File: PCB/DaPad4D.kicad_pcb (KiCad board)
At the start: 2 copper layers, 100 x 19.1 mm, 14 parts, among them J1 Conn_01x12, SW1 SW_Push, SW2 SW_Push, SW3 SW_Push, SW4 SW_Push, SW5 Rotary_Encoder_Switch

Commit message: Moved files
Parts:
- added C3: C, Capacitor_SMD:C_0805_2012Metric_Pad1.15x1.40mm_HandSolder, F.Cu at (137.0, 65.0)
- added C4: C, Capacitor_SMD:C_0805_2012Metric_Pad1.15x1.40mm_HandSolder, F.Cu at (141.8, 65.0)
- added D7: 1N4148W, Diode_SMD:D_SOD-123, F.Cu at (136.5, 56.7)
- added H1: Hole, MountingHole:MountingHole_2.7mm_M2.5, B.Cu at (66.3, 64.0)
- added H2: Hole, MountingHole:MountingHole_2.7mm_M2.5, B.Cu at (123.8, 64.0)
- moved C2 11.5 mm to (141.8, 65.0), turned to 0 degrees
- moved C1 5.86 mm to (137.0, 65.0), turned to 0 degrees
- moved D2 5.38 mm to (136.5, 56.7), turned to 0 degrees
- moved J1 1.88 mm to (130.3, 67.3)
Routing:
- net Col5: track 3.32 -> 6.66 mm, vias 0 -> 1
- net VCC: track 87.4 -> 90.3 mm
- net Net-(D2-Pad2): track 12.0 -> 10.1 mm
- net Col2: track 61.4 -> 63.3 mm
- net Col1: track 79.8 -> 81.7 mm
- net RGB_IN: track 14.1 -> 16.0 mm
- net Row1: track 61.9 -> 60.3 mm
- net RGB_OUT: track 86.7 -> 88.3 mm
- net D1: track 18.6 -> 20.1 mm, vias 0 -> 1
- net Col3: track 42.8 -> 44.2 mm
- net D0: track 11.1 -> 11.8 mm, vias 0 -> 1
- net Col4: track 23.9 -> 24.6 mm
- net Net-(C1-Pad2): track 12.1 -> 11.4 mm

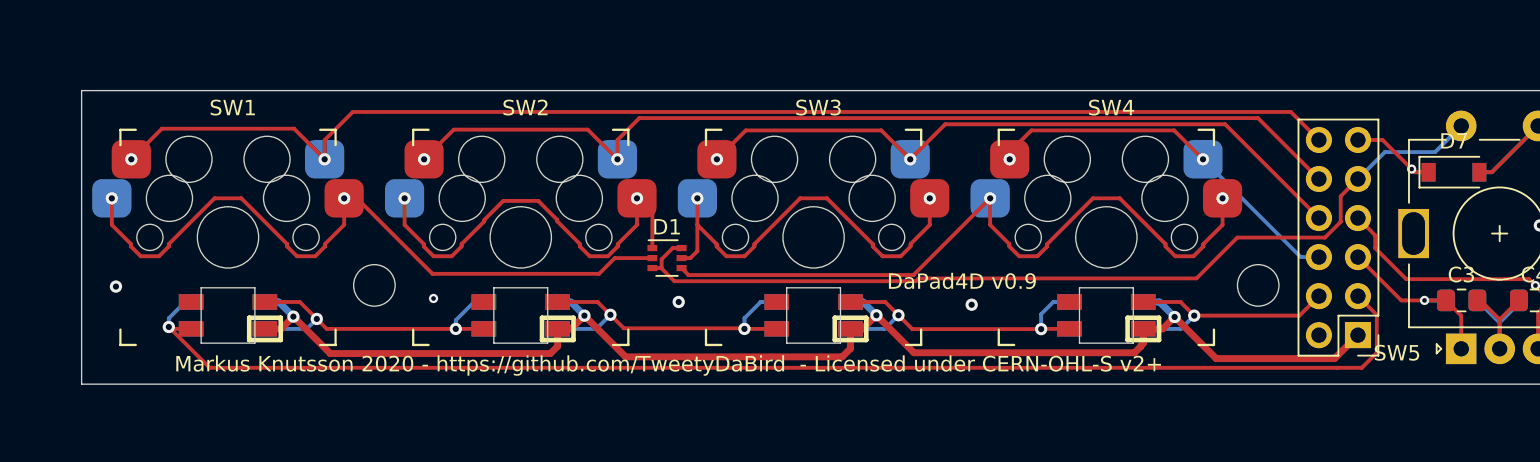
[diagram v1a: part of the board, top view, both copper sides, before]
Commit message: Cleaned up library dependencies
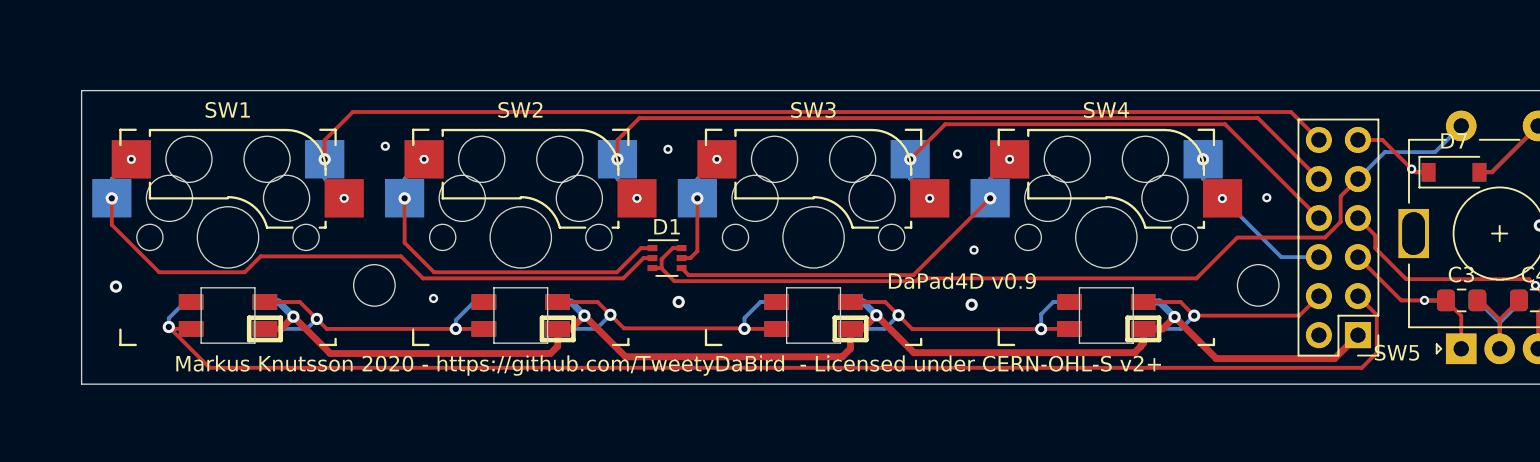
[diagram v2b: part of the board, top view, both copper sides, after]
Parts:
- D3, D4, D5, D6: footprint Keyboard Library:SK6812MINI_rev -> Keyboard Library:SK6812MINI_Midmount_Reversible
- SW1, SW2, SW3, SW4: footprint Keyboard Library:Kailh_socket_MX_reversible_1.0u -> keyswitches:Kailh_socket_MX_reversible_RGB
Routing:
- net Net-(D1-Pad4): track 46.1 -> 25.4 mm
- net Net-(D1-Pad5): track 26.7 -> 7.71 mm
- net Col4: track 24.6 -> 10.9 mm
- net Col1: track 81.7 -> 70.5 mm
- net Col2: track 63.3 -> 52.2 mm
- net Col3: track 44.2 -> 33.1 mm
- net Net-(D1-Pad1): track 27.4 -> 23.5 mm
- net Net-(D1-Pad2): track 46.3 -> 42.8 mm
- net GND: vias 5 -> 10
